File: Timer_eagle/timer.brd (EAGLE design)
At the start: 100 x 80 mm, 22 parts, among them IC1 NE555, IC2 4081N, IC3 4518N, IC4 4070N, IC5 4070N, K1 G5L, Q1 BC548, Q2 TIP120, X1 SSW-103-02-S-S

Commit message: O projeto da plva está atualizado
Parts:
- removed IC5: 4070N, 40xx:DIL14
- moved R6 190.4 mm to (46.3, 42.8), turned to 270 degrees
- moved SV1 167.7 mm to (63.7, 47.2)
- moved R5 165.9 mm to (31.3, 37.0), turned to 270 degrees
- moved C2 146.9 mm to (80.4, 24.3)
- moved C1 121.0 mm to (80.3, 19.1)
- moved R2 119.5 mm to (81.8, 10.4), turned to 180 degrees
- moved R4 103.5 mm to (49.7, 9.04), turned to 180 degrees
- moved IC1 100.8 mm to (70.8, 10.3), turned to 90 degrees
- moved IC2 99.2 mm to (76.2, 36.9), turned to 270 degrees
- moved IC4 97.7 mm to (54.2, 35.2), turned to 270 degrees
- moved LED1 92.9 mm to (38.7, 38.7), turned to 180 degrees
- moved IC3 90.9 mm to (50.6, 17.5)
- moved R3 89.8 mm to (27.0, 37.0), turned to 270 degrees
- moved R1 88.0 mm to (32.0, 15.7), turned to 90 degrees
- moved SW1 82.9 mm to (31.4, 26.3)
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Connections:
- net GND: now also LED1.K
- net N$13: no longer IC5.9
- net N$14: no longer IC5.10
- net N$16: now also Q2.C
- net N$19: now also X1.1; no longer X1.2
- net N$20: now also X1.2; no longer X1.1
- net N$22: now also R5.2
- net N$24: now also Q1.E
- net VCC: no longer IC5.8
- net VDD: no longer IC5.14
- net VSS: no longer IC5.7
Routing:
- net GND: track 0.00 -> 173.0 mm
- net VCC: track 0.00 -> 151.5 mm
- net RESET_555: track 0.00 -> 124.5 mm, vias 0 -> 1
- net VDD: track 0.00 -> 92.8 mm, vias 0 -> 4
- net N$8: track 0.00 -> 75.8 mm, vias 0 -> 3
- net N$9: track 0.00 -> 56.7 mm
- net VSS: track 0.00 -> 44.5 mm, vias 0 -> 2
- net N$6: track 0.00 -> 39.9 mm
- net N$11: track 0.00 -> 37.5 mm
- net N$2: track 0.00 -> 34.2 mm
- net N$10: track 0.00 -> 27.4 mm, vias 0 -> 2
- net N$16: track 0.00 -> 26.7 mm
- net N$4: track 0.00 -> 26.3 mm
- net N$3: track 0.00 -> 26.3 mm
- net N$18: track 0.00 -> 24.8 mm
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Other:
- board size 100 x 80 mm -> 100 x 50 mm

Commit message: O projeto da placa está atualizado
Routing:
- net N$19: track 16.4 -> 22.5 mm
- net N$20: track 19.7 -> 23.5 mm
- net N$8: track 75.8 -> 75.2 mm
- net VDD: track 92.8 -> 93.3 mm
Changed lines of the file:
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@@
 <wire x1="79.875" y1="44.5" x2="79.99" y2="44.48" width="0.4" layer="16"/>
 <wire x1="41" y1="20.625" x2="41.625" y2="21.25" width="0.8128" layer="16"/>
-<wire x1="33.5" y1="20.625" x2="39.375" y2="20.625" width="0.8128" layer="16"/>
+<wire x1="34.5" y1="20.625" x2="39.375" y2="20.625" width="0.8128" layer="16"/>
 <wire x1="39.375" y1="20.625" x2="41" y2="20.625" width="0.8128" layer="16"/>
-<wire x1="20.375" y1="7.5" x2="33.5" y2="20.625" width="0.8128" layer="1"/>
+<wire x1="20.375" y1="7.5" x2="34.5" y2="20.625" width="0.8128" layer="1"/>
 <wire x1="13.25" y1="7.5" x2="20.375" y2="7.5" width="0.8128" layer="16"/>
 <wire x1="41.625" y1="21.25" x2="41.74" y2="21.29" width="0.8128" layer="16"/>
@@
 <wire x1="56.625" y1="41.375" x2="57.875" y2="42.625" width="0.4" layer="16"/>
 <wire x1="48.125" y1="41.375" x2="56.625" y2="41.375" width="0.4" layer="16"/>
-<wire x1="45.75" y1="39" x2="48.125" y2="41.375" width="0.4" layer="16"/>
-<wire x1="45.75" y1="38.75" x2="45.75" y2="39" width="0.4" layer="1"/>
-<wire x1="39.375" y1="32.375" x2="45.75" y2="38.75" width="0.8128" layer="1"/>
+<wire x1="44.25" y1="40.5" x2="48.125" y2="41.375" width="0.4" layer="16"/>
+<wire x1="44.25" y1="40.25" x2="44.25" y2="40.5" width="0.4" layer="1"/>
+<wire x1="39.375" y1="32.375" x2="44.25" y2="40.25" width="0.8128" layer="1"/>
 <wire x1="39.375" y1="24.375" x2="39.375" y2="32.375" width="0.8128" layer="1"/>
 <wire x1="39.375" y1="20.625" x2="39.375" y2="24.375" width="0.8128" layer="16"/>
 <wire x1="57.875" y1="42.625" x2="57.99" y2="42.8" width="0.4" layer="16"/>
-<via x="33.5" y="20.625" extent="1-16" drill="0.6096"/>
+<via x="34.5" y="20.625" extent="1-16" drill="0.6096"/>
 <via x="20.375" y="7.5" extent="1-16" drill="0.6096"/>
-<via x="45.75" y="39" extent="1-16" drill="0.6096"/>
+<via x="44.25" y="40.5" extent="1-16" drill="0.6096"/>
 <via x="39.375" y="24.375" extent="1-16" drill="0.6096"/>
 </signal>
@@
 <wire x1="46.375" y1="19.5" x2="52.625" y2="19.5" width="0.4" layer="16"/>
 <wire x1="45.75" y1="20.125" x2="46.375" y2="19.5" width="0.4" layer="16"/>
-<wire x1="45.75" y1="24.75" x2="45.75" y2="20.125" width="0.4" layer="16"/>
-<wire x1="48.875" y1="24.75" x2="45.75" y2="24.75" width="0.4" layer="16"/>
-<wire x1="59.875" y1="24.75" x2="48.875" y2="24.75" width="0.4" layer="1"/>
+<wire x1="45.75" y1="23.75" x2="45.75" y2="20.125" width="0.4" layer="16"/>
+<wire x1="46.875" y1="24.75" x2="45.75" y2="23.75" width="0.4" layer="16"/>
+<wire x1="59.875" y1="24.75" x2="46.875" y2="24.75" width="0.4" layer="1"/>
 <wire x1="69.75" y1="34.625" x2="68.75" y2="33.625" width="0.4" layer="1"/>
 <wire x1="68.75" y1="33.625" x2="59.875" y2="24.75" width="0.4" layer="1"/>
@@
 <wire x1="68.875" y1="33.5" x2="68.875" y2="24.375" width="0.4" layer="1"/>
 <wire x1="68.875" y1="33.5" x2="68.75" y2="33.625" width="0.4" layer="1"/>
-<via x="48.875" y="24.75" extent="1-16" drill="0.6096"/>
+<via x="46.875" y="24.75" extent="1-16" drill="0.6096"/>
 <via x="69.75" y="41.875" extent="1-16" drill="0.6096"/>
 <via x="68.875" y="24.375" extent="1-16" drill="0.6096"/>
@@
 <contactref element="K1" pad="S"/>
 <contactref element="X1" pad="2"/>
-<wire x1="3.875" y1="41.125" x2="2.25" y2="42.75" width="0.4" layer="16"/>
-<wire x1="17.625" y1="41.125" x2="3.875" y2="41.125" width="0.4" layer="16"/>
-<wire x1="20" y1="43.5" x2="17.625" y2="41.125" width="0.4" layer="16"/>
+<wire x1="6.875" y1="39.625" x2="2.25" y2="42.75" width="1.6764" layer="16"/>
+<wire x1="20.625" y1="39.625" x2="6.875" y2="39.625" width="1.6764" layer="16"/>
+<wire x1="20" y1="43.5" x2="20.625" y2="39.625" width="1.6764" layer="16"/>
 <wire x1="2.25" y1="42.75" x2="2.19" y2="42.85" width="0.4" layer="16"/>
 <wire x1="20" y1="43.5" x2="20.079" y2="43.599" width="0.4" layer="16"/>
@@
 <contactref element="X1" pad="3"/>
 <contactref element="K1" pad="O"/>
-<wire x1="4" y1="43.625" x2="2.25" y2="45.375" width="0.4" layer="16"/>
-<wire x1="8.125" y1="43.625" x2="4" y2="43.625" width="0.4" layer="16"/>
+<wire x1="5" y1="46.125" x2="2.25" y2="45.375" width="1.6764" layer="16"/>
+<wire x1="8.125" y1="43.625" x2="5" y2="46.125" width="1.6764" layer="16"/>
 <wire x1="2.25" y1="45.375" x2="2.19" y2="45.39" width="0.4" layer="16"/>
 <wire x1="8.125" y1="43.625" x2="8.141" y2="43.599" width="0.4" layer="16"/>
@@
 <contactref element="K1" pad="P"/>
 <contactref element="X1" pad="1"/>
-<wire x1="8.625" y1="33.875" x2="2.19" y2="40.31" width="0.4" layer="16"/>
-<wire x1="9.5" y1="33.875" x2="8.625" y2="33.875" width="0.4" layer="16"/>
-<wire x1="14" y1="29.375" x2="9.5" y2="33.875" width="0.4" layer="16"/>
+<wire x1="14.625" y1="33.875" x2="2" y2="35.5" width="1.6764" layer="16"/>
+<wire x1="2" y1="35.5" x2="2" y2="40.31" width="1.6764" layer="16"/>
+<wire x1="2" y1="40.31" x2="2.19" y2="40.31" width="1.6764" layer="16"/>
+<wire x1="14.5" y1="33.875" x2="14.625" y2="33.875" width="1.6764" layer="16"/>
+<wire x1="14" y1="29.375" x2="14.5" y2="33.875" width="1.6764" layer="16"/>
 <wire x1="14" y1="29.375" x2="14.11" y2="29.375" width="0.4" layer="16"/>
 </signal>

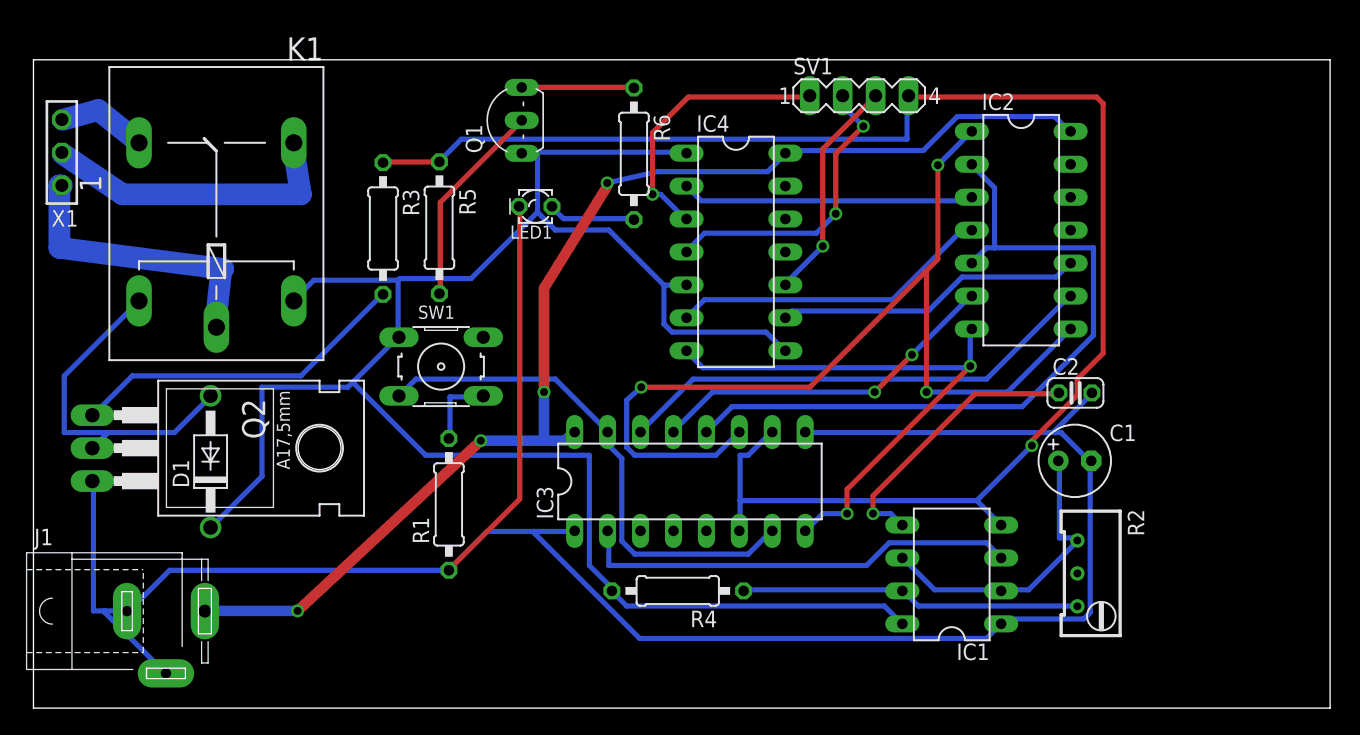
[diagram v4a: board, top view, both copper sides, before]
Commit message: As trilhas de alimentação foram engrssadas, e a placa foi completada com o terra
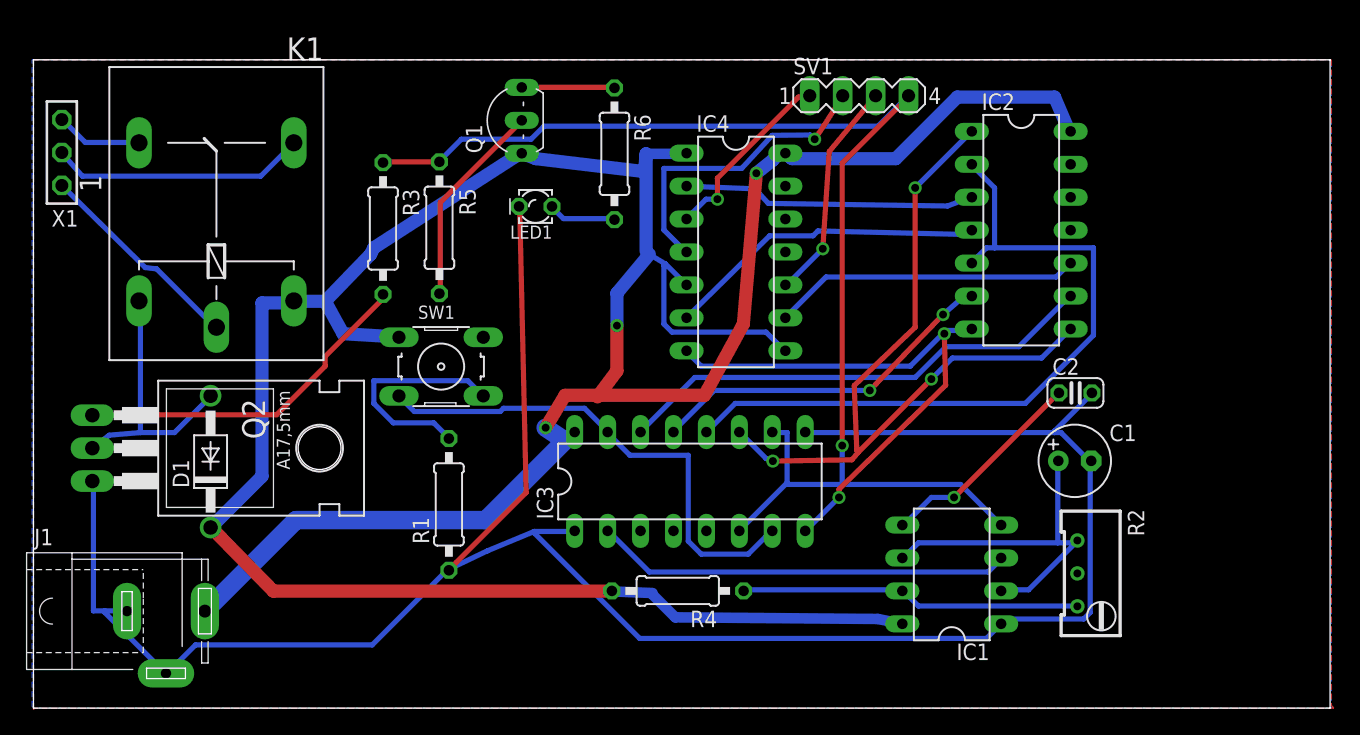
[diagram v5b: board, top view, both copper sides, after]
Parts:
- moved R6 1.50 mm to (44.8, 42.8)
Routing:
- net RESET_555: track 124.5 -> 102.9 mm
- net N$8: track 75.2 -> 59.2 mm
- net N$5: track 5.85 -> 17.6 mm
- net VCC: track 151.5 -> 160.5 mm, vias 0 -> 1
- net N$12: track 21.4 -> 14.4 mm
- net N$19: track 22.5 -> 16.4 mm
- net N$16: track 26.7 -> 20.9 mm
- net N$7: track 21.6 -> 16.3 mm
- net N$1: track 23.7 -> 27.9 mm
- net N$20: track 23.5 -> 19.8 mm
- net VDD: track 93.3 -> 96.3 mm, vias 4 -> 2
- net N$2: track 34.2 -> 32.1 mm
- net GND: track 173.0 -> 171.6 mm
- net N$6: track 39.9 -> 38.7 mm
- net VSS: track 44.5 -> 43.5 mm
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- added copper zone on layer 1, net GND
- added copper zone on layer 16, net GND

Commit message: Projeto final da placa
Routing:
- net N$12: track 14.4 -> 21.1 mm
- net RESET_555: track 102.9 -> 106.9 mm
- net N$8: track 59.2 -> 62.4 mm
- net N$19: track 16.4 -> 19.5 mm
- net GND: track 171.6 -> 174.7 mm
- net N$9: track 56.7 -> 59.3 mm
- net N$25: track 0.00 -> 2.41 mm, vias 0 -> 1
- net N$26: track 0.00 -> 2.37 mm
- net N$20: track 19.8 -> 22.0 mm
- net N$5: track 17.6 -> 19.6 mm
- net VDD: track 96.3 -> 98.1 mm
- net VSS: track 43.5 -> 45.3 mm
- net N$10: track 27.4 -> 29.2 mm
- net VCC: track 160.5 -> 161.9 mm
- net N$6: track 38.7 -> 40.0 mm
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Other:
- board text added: "ADA"
